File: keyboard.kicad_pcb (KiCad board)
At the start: 2 copper layers, 285 x 94.6 mm, 255 parts, among them IC1 ATMEGA32U4, J1 USB_2, P1 DIL16, P2 DIL16, P3 CONN_6, SW1 SW_PUSH, X1 ASX4

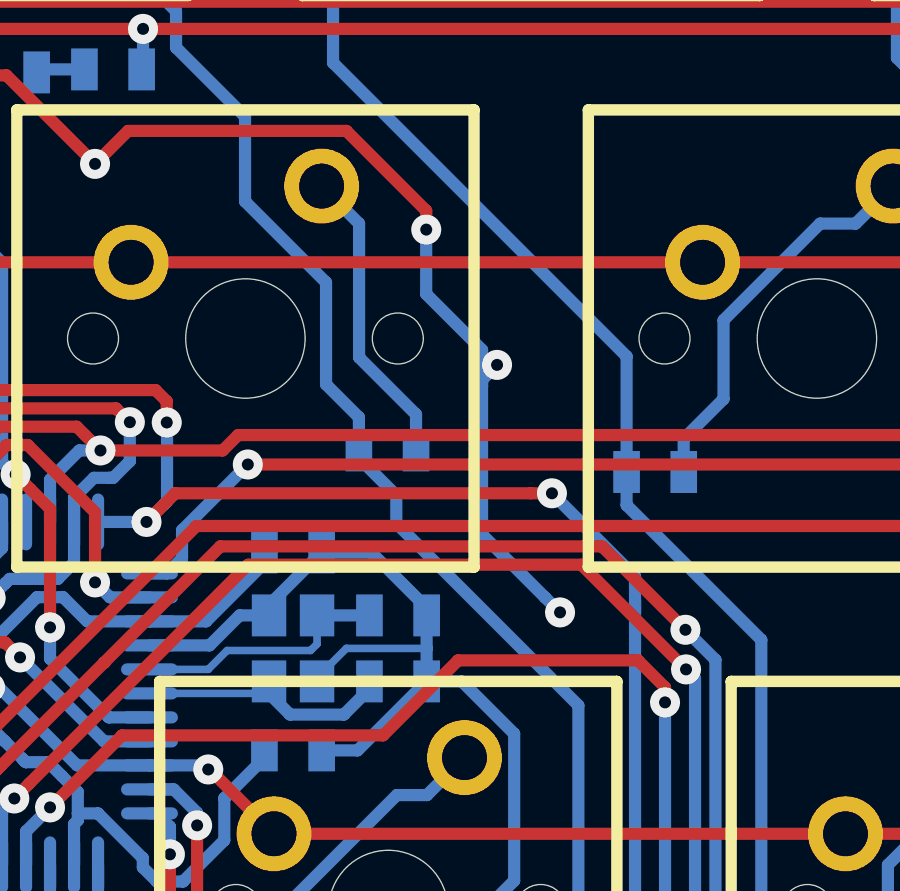
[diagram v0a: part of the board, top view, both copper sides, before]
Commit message: align diode
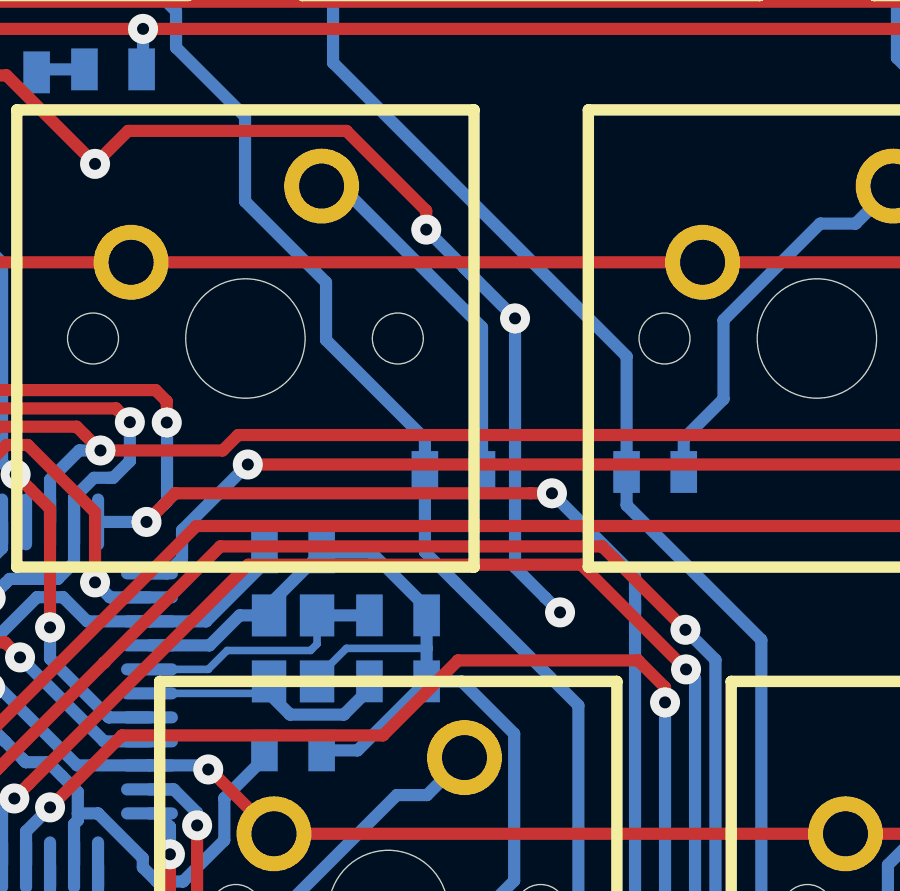
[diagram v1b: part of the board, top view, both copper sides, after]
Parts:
- moved D7 2.31 mm to (106.9, 97.3)
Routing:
- net Net-(D7-Pad2): track 10.4 -> 12.1 mm
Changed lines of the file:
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@@
     (thickness 1.6002)
     (drawings 283)
-    (tracks 2383)
+    (tracks 2382)
     (zones 0)
     (modules 255)
@@
   )
   (module 0805:0805D (layer B.Cu)
-    (at 104.7475 96.6)
+    (at 106.9475 97.32)
     (attr smd)
     (fp_text reference D7 (at 0 1.775) (layer B.SilkS)
@@
   (segment (start 66.404501 141.621521) (end 86.978479 141.621521) (width 0.4064) (layer F.Cu) (net 1))
   (segment (start 82.73586 82.296) (end 83.388262 81.643598) (width 0.4064) (layer F.Cu) (net 1))
+  (via (at 109 92.2) (size 1) (drill 0.4) (layers F.Cu B.Cu) (net 2))
+  (segment (start 106.04 89.24) (end 107.3 90.5) (width 0.4064) (layer B.Cu) (net 2))
+  (segment (start 107.3 90.5) (end 107.65 90.85) (width 0.4064) (layer B.Cu) (net 2))
+  (segment (start 109 94.35) (end 109 92.2) (width 0.4064) (layer B.Cu) (net 2))
+  (segment (start 109 92.2) (end 107.3 90.5) (width 0.4064) (layer B.Cu) (net 2))
+  (segment (start 109 100.5) (end 110.000001 101.500001) (width 0.4064) (layer B.Cu) (net 2))
+  (segment (start 109 100.5) (end 109 94.35) (width 0.4064) (layer B.Cu) (net 2))
   (segment (start 156.37475 141.47341) (end 155.22 141.47341) (width 0.254) (layer B.Cu) (net 2))
   (segment (start 153.409071 141.240929) (end 154.116177 141.240929) (width 0.4064) (layer B.Cu) (net 2))
@@
   (segment (start 174.638969 106.748995) (end 174.638969 107.27) (width 0.4064) (layer F.Cu) (net 2))
   (via (at 174.638969 107.27) (size 1) (drill 0.4) (layers F.Cu B.Cu) (net 2))
-  (segment (start 107.900001 94.249999) (end 107.900001 94.47) (width 0.4064) (layer B.Cu) (net 2))
-  (segment (start 107.900001 94.47) (end 107.900001 99.400001) (width 0.4064) (layer B.Cu) (net 2))
-  (segment (start 106.04 89.24) (end 106.04 91.39) (width 0.4064) (layer B.Cu) (net 2))
-  (segment (start 106.04 91.39) (end 107.900001 93.250001) (width 0.4064) (layer B.Cu) (net 2))
-  (segment (start 107.900001 93.250001) (end 107.900001 94.47) (width 0.4064) (layer B.Cu) (net 2))
   (segment (start 106.04 88.61) (end 106.04 89.24) (width 0.4064) (layer F.Cu) (net 2))
   (via (at 106.04 89.24) (size 1) (drill 0.4) (layers F.Cu B.Cu) (net 2))
@@
   (segment (start 267.541101 155.028899) (end 271.001101 155.028899) (width 0.4064) (layer B.Cu) (net 2))
   (segment (start 110.000001 101.500001) (end 110.5 102) (width 0.4064) (layer B.Cu) (net 2))
-  (segment (start 107.900001 99.400001) (end 110.000001 101.500001) (width 0.4064) (layer B.Cu) (net 2))
-  (segment (start 108.4 93.75) (end 107.900001 94.249999) (width 0.4064) (layer B.Cu) (net 2))
   (via (at 63.3 116.6) (size 1) (drill 0.4) (layers F.Cu B.Cu) (net 2))
   (segment (start 72.898 126.492) (end 74.168 125.222) (width 0.4064) (layer B.Cu) (net 2))
@@
   (segment (start 129 108) (end 128.500001 108.499999) (width 0.4064) (layer B.Cu) (net 2))
   (segment (start 128.500001 108.499999) (end 128.500001 109.799999) (width 0.4064) (layer B.Cu) (net 2))
-  (via (at 108.4 93.75) (size 1) (drill 0.4) (layers F.Cu B.Cu) (net 2))
   (segment (start 95 87.05) (end 96.1 85.95) (width 0.4064) (layer F.Cu) (net 2))
   (segment (start 92.049999 84.099999) (end 95 87.05) (width 0.4064) (layer F.Cu) (net 2))
@@
   (segment (start 67.483989 113.925349) (end 68.78574 115.2271) (width 0.4064) (layer B.Cu) (net 4))
   (segment (start 68.78574 115.2271) (end 68.78574 116.332) (width 0.4064) (layer B.Cu) (net 4) (status 20))
+  (segment (start 102.7 92.5) (end 102.7 91) (width 0.4064) (layer B.Cu) (net 5))
+  (segment (start 105.995 96.2151) (end 102.7 92.9201) (width 0.4064) (layer B.Cu) (net 5))
+  (segment (start 105.995 97.32) (end 105.995 96.2151) (width 0.4064) (layer B.Cu) (net 5))
+  (segment (start 102.7 92.9201) (end 102.7 92.5) (width 0.4064) (layer B.Cu) (net 5))
+  (segment (start 107 100.988969) (end 111.111031 105.1) (width 0.4064) (layer B.Cu) (net 5))
+  (segment (start 107 100.988969) (end 105.995 99.983969) (width 0.4064) (layer B.Cu) (net 5))
+  (segment (start 105.995 99.983969) (end 105.995 97.32) (width 0.4064) (layer B.Cu) (net 5))
   (segment (start 82.2 116.5) (end 82.2 114.46702) (width 0.4064) (layer B.Cu) (net 5))
   (segment (start 78.82 107.55) (end 78.82 105.22) (width 0.4064) (layer B.Cu) (net 5))
@@
   (segment (start 100 88.3) (end 100 85.472978) (width 0.4064) (layer B.Cu) (net 5))
   (segment (start 102.7 91) (end 100 88.3) (width 0.4064) (layer B.Cu) (net 5))
-  (segment (start 103.795 96.6) (end 103.795 95.4951) (width 0.4064) (layer B.Cu) (net 5) (status 10))
   (segment (start 95.595 79.854) (end 97.7 81.959) (width 0.4064) (layer B.Cu) (net 5) (status 10))
-  (segment (start 102.7 94.4001) (end 102.7 91) (width 0.4064) (layer B.Cu) (net 5))
   (segment (start 97.7 83.172978) (end 97.7 81.959) (width 0.4064) (layer B.Cu) (net 5))
-  (segment (start 103.795 95.4951) (end 102.7 94.4001) (width 0.4064) (layer B.Cu) (net 5))
   (via (at 108.920592 120.59359) (size 1) (drill 0.4) (layers F.Cu B.Cu) (net 5))
   (segment (start 102.26802 120.6) (end 108.914182 120.6) (width 0.4064) (layer F.Cu) (net 5))
   (segment (start 109.420591 120.093591) (end 108.920592 120.59359) (width 0.4064) (layer B.Cu) (net 5))
   (segment (start 111.111031 118.403151) (end 109.420591 120.093591) (width 0.4064) (layer B.Cu) (net 5))
-  (segment (start 105.041 99.029969) (end 111.111031 105.1) (width 0.4064) (layer B.Cu) (net 5))
   (segment (start 111.111031 105.1) (end 111.111031 118.403151) (width 0.4064) (layer B.Cu) (net 5))
-  (segment (start 103.795 96.854) (end 105.041 98.1) (width 0.4064) (layer B.Cu) (net 5))
-  (segment (start 105.041 98.1) (end 105.041 99.029969) (width 0.4064) (layer B.Cu) (net 5))
   (segment (start 108.914182 120.6) (end 108.920592 120.59359) (width 0.4064) (layer F.Cu) (net 5))
   (segment (start 82.2 116.5) (end 84.5 116.5) (width 0.4064) (layer F.Cu) (net 5))
@@
   (segment (start 90.513564 78.1) (end 89.714814 78.89875) (width 0.4064) (layer B.Cu) (net 86))
   (segment (start 89.714814 78.89875) (end 87.9475 78.89875) (width 0.4064) (layer B.Cu) (net 86))
-  (segment (start 103.802179 93.502179) (end 105.7 95.4) (width 0.4064) (layer B.Cu) (net 87))
-  (segment (start 105.7 95.4) (end 105.7 96.6) (width 0.4064) (layer B.Cu) (net 87) (status 20))
-  (segment (start 102.5525 87.79002) (end 103.802179 89.039699) (width 0.4064) (layer B.Cu) (net 87) (status 10))
-  (segment (start 103.802179 89.039699) (end 103.802179 93.502179) (width 0.4064) (layer B.Cu) (net 87))
-  (segment (start 105.7 96.6) (end 105.7 96.346) (width 0.4064) (layer B.Cu) (net 87) (status 30))
+  (segment (start 107.9 93.13752) (end 107.9 92.5) (width 0.4064) (layer B.Cu) (net 87))
+  (segment (start 103.19002 87.79002) (end 102.5525 87.79002) (width 0.4064) (layer B.Cu) (net 87))
+  (segment (start 107.9 92.5) (end 103.19002 87.79002) (width 0.4064) (layer B.Cu) (net 87))
+  (segment (start 107.9 97.32) (end 107.9 93.13752) (width 0.4064) (layer B.Cu) (net 87))
   (segment (start 102.04958 116.39042) (end 102.04958 116.13642) (width 0.4064) (layer B.Cu) (net 88))
   (segment (start 102.04958 116.13642) (end 100.95 115.03684) (width 0.4064) (layer B.Cu) (net 88))

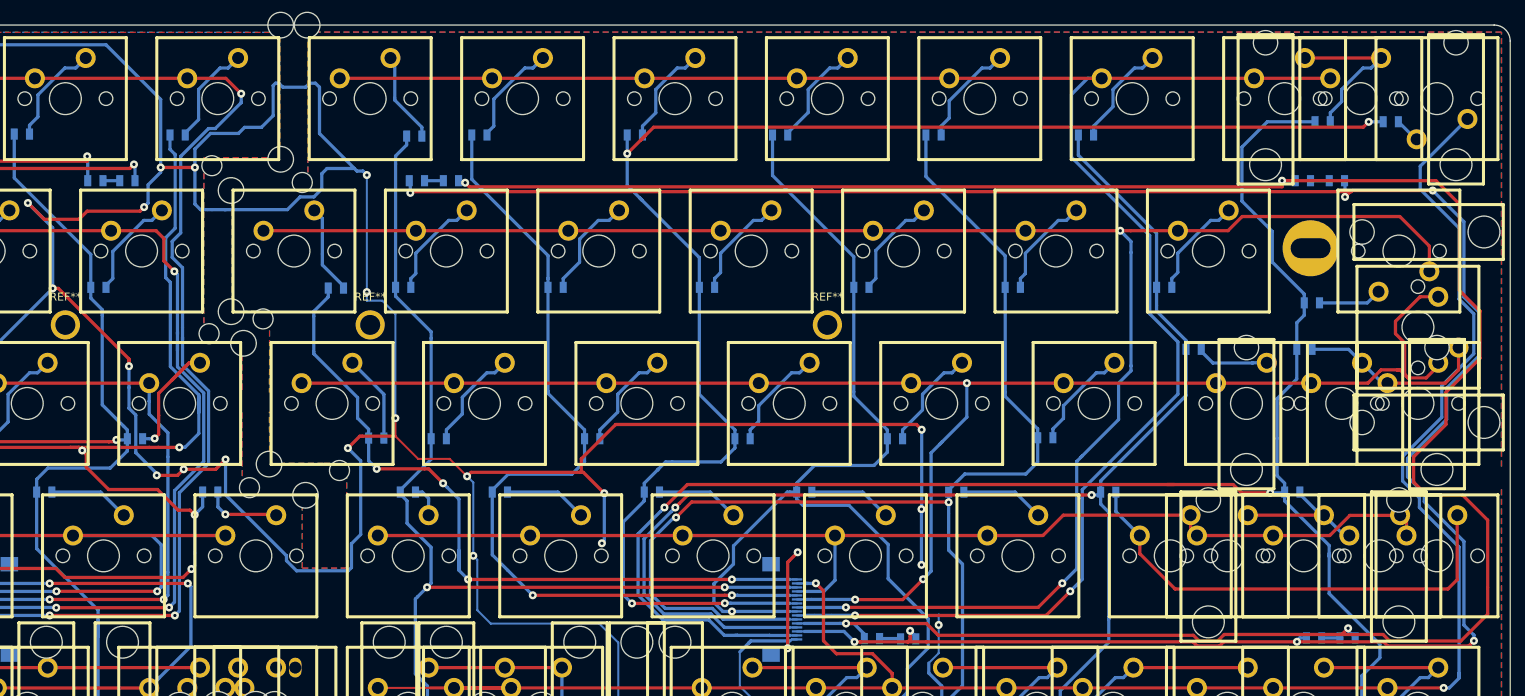
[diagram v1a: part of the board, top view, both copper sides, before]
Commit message: adjust diode position and track
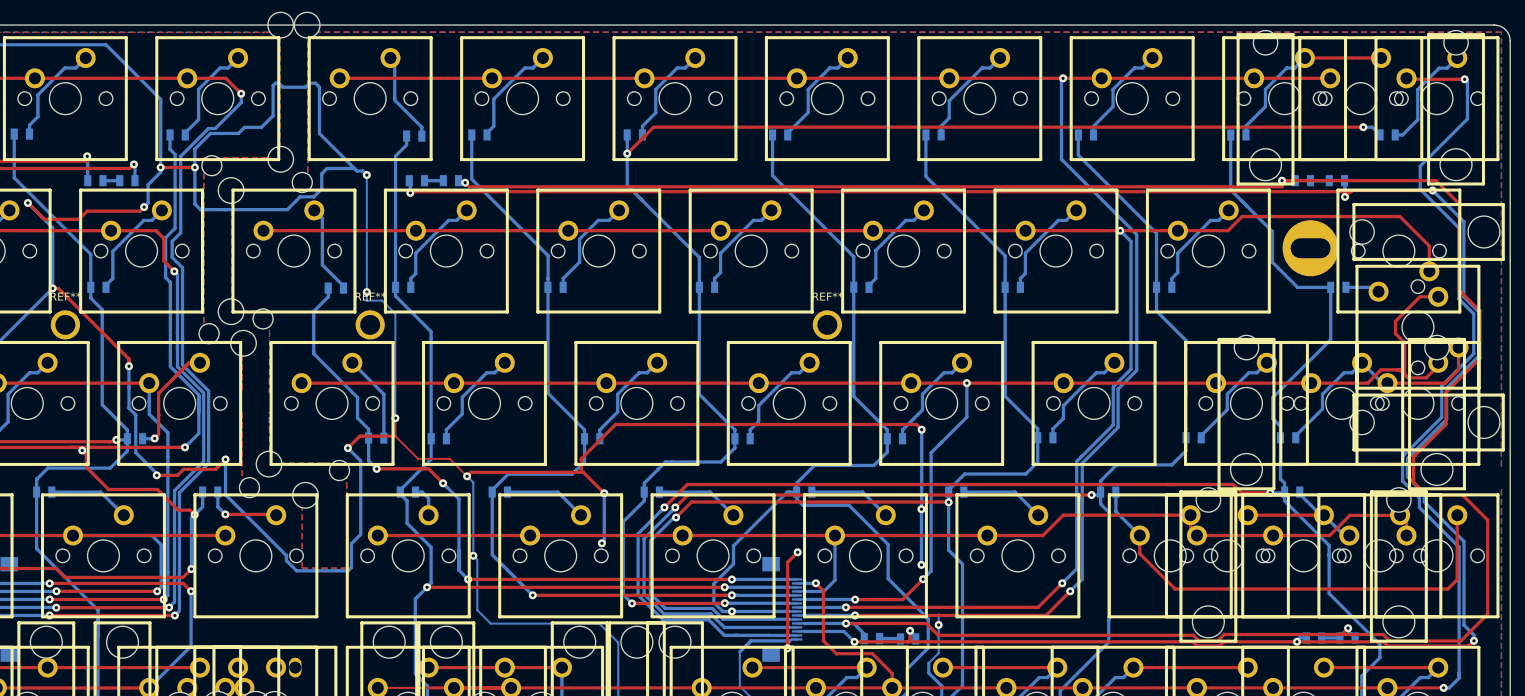
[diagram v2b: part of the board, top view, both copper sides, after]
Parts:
- moved D68 11.2 mm to (319.5, 116.2)
- moved D63 11.0 mm to (307.7, 116.2)
- moved D66 10.7 mm to (313.3, 78.4)
- moved D67 3.83 mm to (325.8, 97.4)
- moved D50 1.69 mm to (332.0, 78.4)
- turned S50 to 0 degrees
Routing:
- net /row5-r: track 247.5 -> 260.0 mm, vias 2 -> 3
- net Net-(D50-Pad2): track 3.19 -> 13.9 mm
- net Net-(D68-Pad2): track 23.5 -> 30.0 mm
- net /row1-r: track 237.4 -> 231.1 mm, vias 2 -> 3
- net /col13-r: track 175.2 -> 179.8 mm
- net Net-(D63-Pad2): track 9.06 -> 13.3 mm
- net Net-(D67-Pad2): track 7.96 -> 4.30 mm
- net Net-(D66-Pad2): track 21.0 -> 22.8 mm
- net /col14-r: track 210.1 -> 208.8 mm
- net GND: vias 54 -> 53

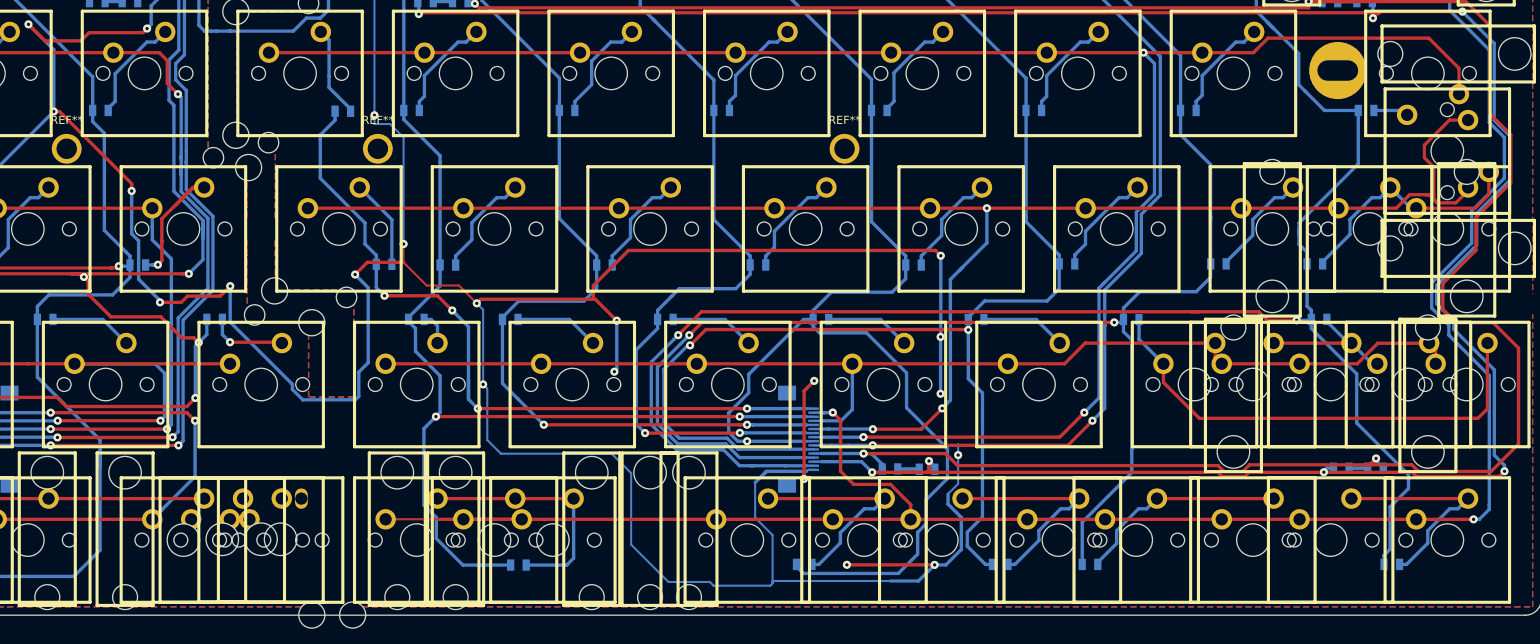
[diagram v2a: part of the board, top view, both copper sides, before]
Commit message: add switch S35 to scan matrix
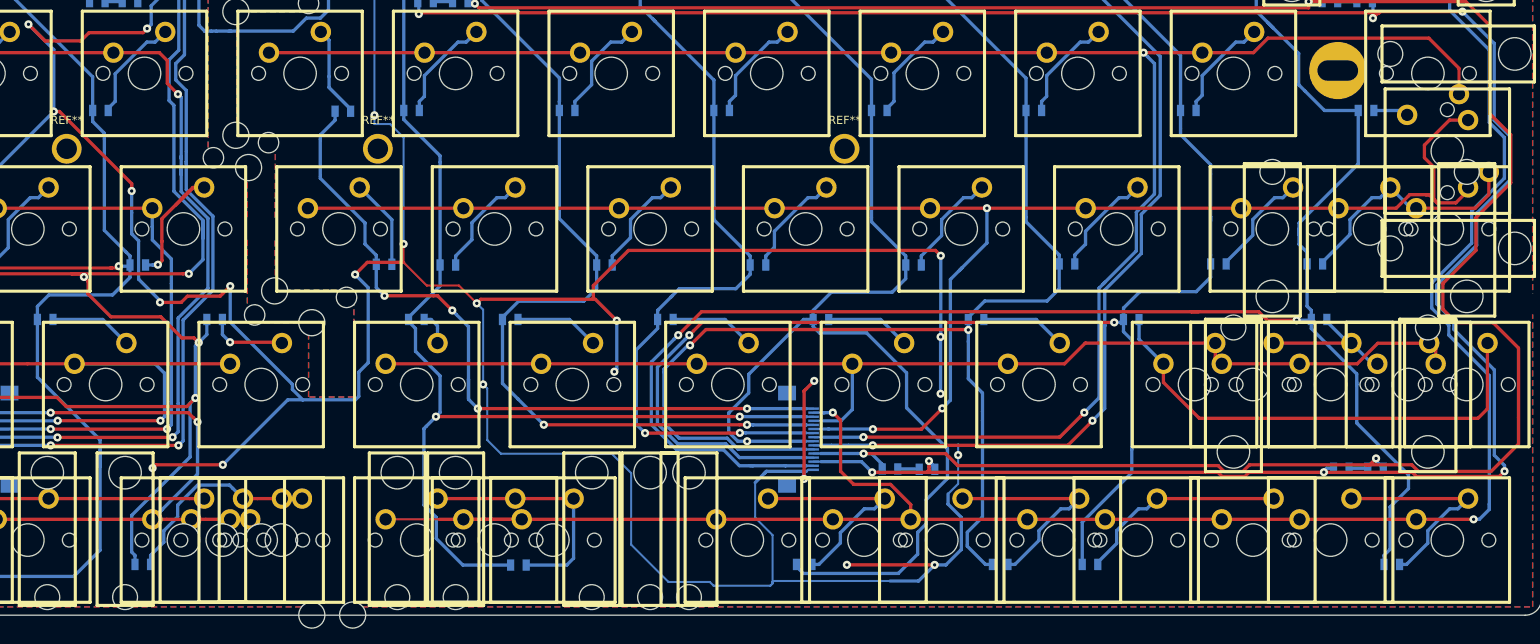
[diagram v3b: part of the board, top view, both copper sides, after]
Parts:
- removed MX1A (x3): VAL**, mx1a:MX1A
- added D35: 1N4148, 0805:0805D, B.Cu at (176.0, 153.0)
- added S35: MX1A, mx1a:MX1A, F.Cu at (190.5, 150.0)
- added S351: MX1A, mx1a:MX1A_no3d, F.Cu at (185.7, 150.0)
- added S352: MX1A, mx1a:MX1A_no3d, F.Cu at (193.0, 150.0)
- moved HOLE 2.50 mm to (185.6, 95.0)
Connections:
- J1 pad 4: (no net) -> GND
- J1 pad 5: GND -> (no net)
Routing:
- net Net-(D35-Pad2): track 0.00 -> 25.6 mm
- net /col7: track 198.2 -> 222.0 mm
- net GND: track 1122.4 -> 1144.3 mm, vias 53 -> 55
- net /row5: track 198.9 -> 211.3 mm
